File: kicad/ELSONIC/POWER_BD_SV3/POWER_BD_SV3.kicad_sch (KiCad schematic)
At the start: 99 parts, among them J2 SMW250-06P, J3 SMW250-02P, T1 EI2811BP, T2 EER28, U1 ICE3BR0665J, U2 H11AA1, U3 PC817, U4 ATTINY85-20PU_1, U5 MOC3021M, U6 LM7805_TO220

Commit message: JLCPCB에 POWER_BD주문
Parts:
- removed C31: MPP104/600V, 04_MyFoot_Passive:C_PP_L23.0mm_W10.9mm_P21.2mm, symbol 04_MyLib_Passive:C
- removed LED1, LED2: RED/3Pi, 03_MyFoot_Active:LED_D3.0mm, symbol 03_MyLib_Active:LED
- removed RV2: 3362P103, symbol Device:R_Potentiometer_US
- added C31: MPP104/600V, 04_MyFoot_Passive:C_PP_P10.0mm_P21.2mm, symbol 04_MyLib_Passive:C_2AB
- added LED1, LED2: LED_SMD, 03_MyFoot_Active:LED_2012Metric, symbol 03_MyLib_Active:LED_SMD
- added RV2: 3362P103, 04_MyFoot_Passive:TRIM_3362P, symbol 04_MyLib_Passive:R_POT
- C11, C13: footprint 04_MyFoot_Passive:C_Disc_D6.0mm_P5.00mm -> 04_MyFoot_Passive:C_3216Metric
- C12, C26, C27, C28, C30, C5, C9: footprint 04_MyFoot_Passive:C_Disc_D4.7mm_T3.0mm_P5.00mm -> 04_MyFoot_Passive:C_3216Metric
- C15, C19, C6, C8: footprint 04_MyFoot_Passive:C_Disc_D4.7mm_P5.00mm -> 04_MyFoot_Passive:C_3216Metric
- C7: value CC472/630V -> CC472/1kV
- D3: value UF4004 -> UF4007
- R10, R11, R12, R14, R15, R16, R17, R2, R21, R22, R23, R27, R6, R7, R8, R9: footprint 04_MyFoot_Passive:R_Axial_0.25W_P10.16mm -> 04_MyFoot_Passive:R_3216Metric
- R13: value 1.2K -> 1.2K/F; footprint 04_MyFoot_Passive:R_Axial_0.25W_P10.16mm -> 04_MyFoot_Passive:R_3216Metric
- R18: value 1K -> 1K/F; footprint 04_MyFoot_Passive:R_Axial_0.25W_P10.16mm -> 04_MyFoot_Passive:R_3216Metric
- R19: value 40K -> 40K/F; footprint 04_MyFoot_Passive:R_Axial_0.25W_P10.16mm -> 04_MyFoot_Passive:R_3216Metric
- R20: value 10K -> 10K/F; footprint 04_MyFoot_Passive:R_Axial_0.25W_P10.16mm -> 04_MyFoot_Passive:R_3216Metric
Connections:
- net +5V: now also RV2.1
- net GND: now also LED1.1 (K), LED2.1 (K), RV2.3
- net N01: now also C31.2, C31.4
- net at R24.2, R25.2: now also C31.1, C31.3
- net at R21.2: now also LED1.2 (A)
- net at R22.1: now also LED2.2 (A)
- net at R27.1: now also RV2.2

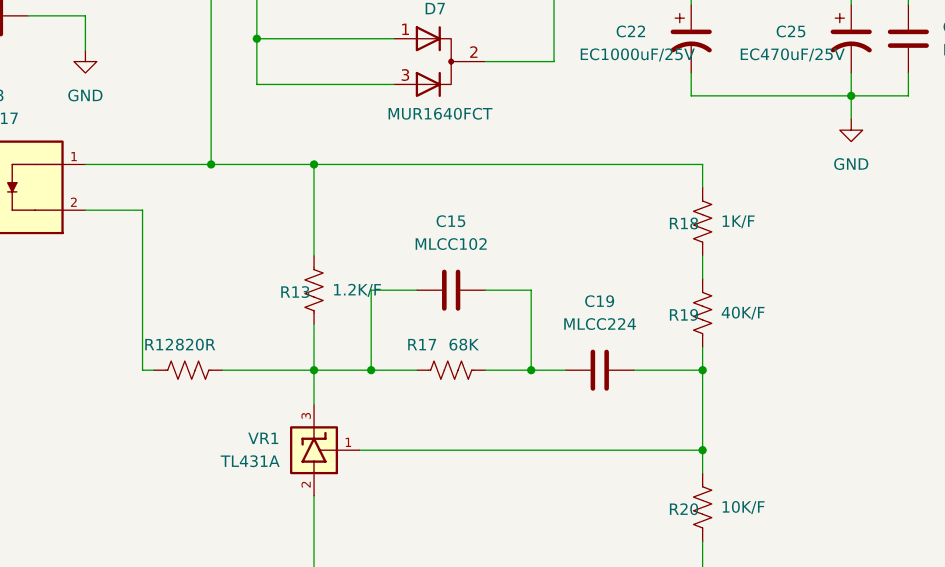
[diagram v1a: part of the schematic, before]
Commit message: Updated dimmer settings and final adjustments made.
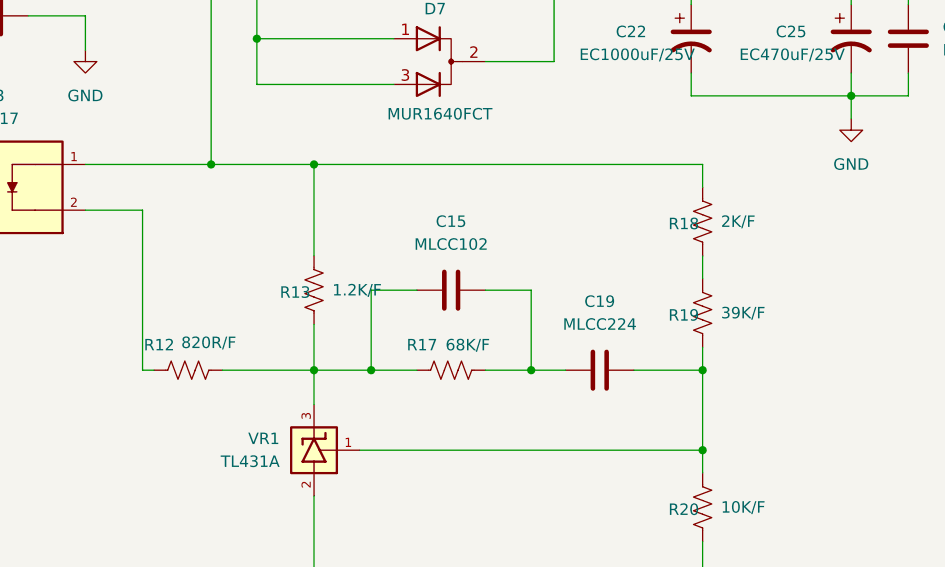
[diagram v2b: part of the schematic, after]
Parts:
- R12: value 820R -> 820R/F
- R17: value 68K -> 68K/F
- R18: value 1K/F -> 2K/F
- R19: value 40K/F -> 39K/F
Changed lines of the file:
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@@
 			)
 		)
-		(property "Value" "40K/F"
+		(property "Value" "39K/F"
 			(at 242.062 127 0)
 			(effects
@@
 			)
 		)
-		(property "Value" "820R"
-			(at 185.928 130.556 90)
+		(property "Value" "820R/F"
+			(at 188.214 130.302 90)
 			(effects
 				(font
@@
 			)
 		)
-		(property "Value" "68K"
-			(at 215.138 130.556 90)
+		(property "Value" "68K/F"
+			(at 216.408 130.556 90)
 			(effects
 				(font
@@
 			)
 		)
-		(property "Value" "1K/F"
+		(property "Value" "2K/F"
 			(at 242.062 116.84 0)
 			(effects

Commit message: ms_board_V3 회로설계 1차 내용정리
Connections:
- net AC12V: now reaches R2.1, T1.4 (SB)
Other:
- moved on the sheet: C8, R2, R6, T1, U2
